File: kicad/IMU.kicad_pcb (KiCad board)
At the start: 4 copper layers, 30 x 30 mm, 85 parts, among them IC1 FT232RQ, P1 M1P, P10 CONN_01X02, P11 CONN_02X05, P12 CONN_02X06, P2 M1N, P3 M3P, P4 M3N, P5 JTAG_DB, P6 M2P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

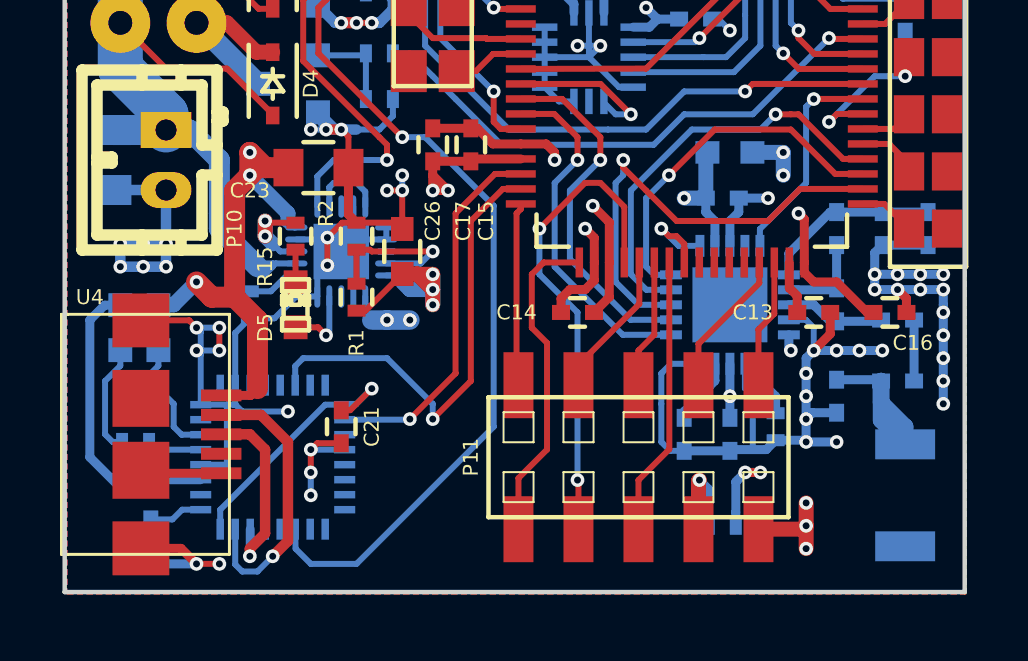
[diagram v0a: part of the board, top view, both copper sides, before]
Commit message: Moved USB and external edge connector and re-routed FTDI IC.
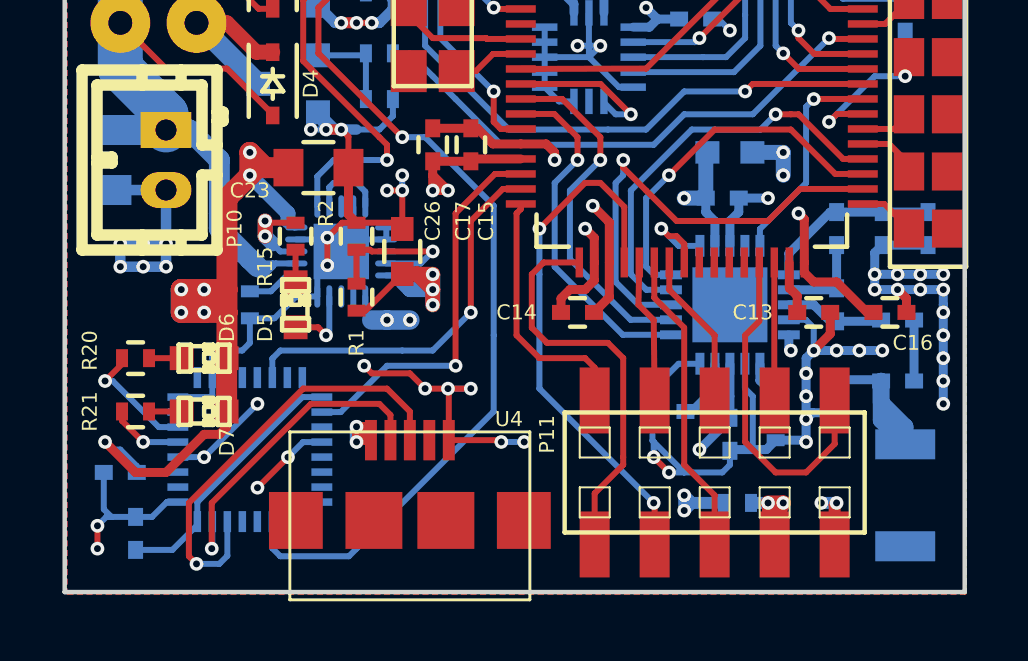
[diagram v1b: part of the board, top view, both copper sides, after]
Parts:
- added G***: LOGO, logos:Panda_Logo_4x3mm, B.Cu at (115.1, 97.3)
- C21: moved to B.Cu
- D6, D7, R20, R21: moved to F.Cu
- moved U4 11.3 mm to (111.5, 99.1), turned to 0 degrees
- moved C21 7.73 mm to (102.4, 98.0), turned to 90 degrees
- moved D7 3.95 mm to (104.6, 94.0), turned to 180 degrees
- moved P11 2.59 mm to (121.7, 96.0)
- moved D6 1.83 mm to (104.6, 92.2), turned to 180 degrees
- moved C22 1.44 mm to (101.9, 96.0), turned to 180 degrees
- moved R20 1.27 mm to (102.4, 92.2), turned to 0 degrees
- moved R21 1.02 mm to (102.4, 94.0), turned to 0 degrees
- moved C2 0.92 mm to (120.1, 94.0), turned to 180 degrees
- moved R16 0.92 mm to (122.4, 97.0), turned to 0 degrees
- moved IC1 0.80 mm to (106.2, 95.2)
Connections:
- P11 pad 10: /Microcontroller/CON_SDA -> /Microcontroller/CON_SCL
- P11 pad 5: /Microcontroller/CON_MOSI -> /Microcontroller/CON_MISO
- P11 pad 6: /Microcontroller/CON_MISO -> /Microcontroller/CON_MOSI
- P11 pad 8: /Microcontroller/CON_SCL -> /Microcontroller/CON_SDA
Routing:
- net +5V: track 29.3 -> 49.0 mm, vias 3 -> 9
- net Net-(IC1-Pad14): track 6.35 -> 14.6 mm
- net /Microcontroller/CON_SCL: track 4.93 -> 11.4 mm
- net /Microcontroller/CON_MISO: track 4.31 -> 10.2 mm
- net GND: track 178.8 -> 174.5 mm, vias 88 -> 90
- net /Microcontroller/CON_MOSI: track 9.32 -> 5.23 mm
- net Net-(C3-Pad1): track 15.7 -> 19.4 mm
- net /Microcontroller/CON_RX: track 10.8 -> 13.6 mm
- net /Power/FTDI_TXD: track 15.7 -> 13.0 mm
- net Net-(D7-Pad2): track 3.69 -> 1.09 mm
- net /Microcontroller/CON_TX: track 6.13 -> 8.58 mm
- net /Microcontroller/CON_DAC: track 16.2 -> 17.8 mm
- net Net-(IC1-Pad15): track 9.35 -> 10.8 mm
- net Net-(IC1-Pad22): track 2.70 -> 4.06 mm, vias 0 -> 1
- net Net-(D6-Pad2): track 2.34 -> 1.09 mm
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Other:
- board text added: "Jonas A 2015"

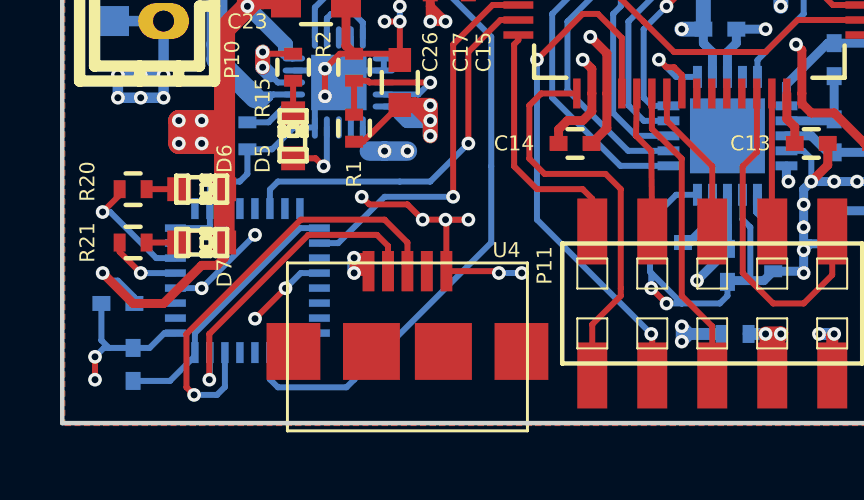
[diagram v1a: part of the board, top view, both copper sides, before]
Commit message: Replaced USB connector footprint.
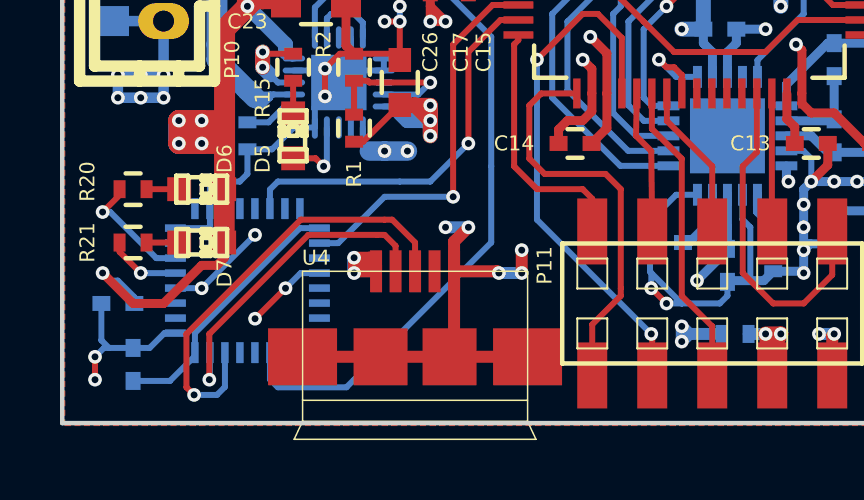
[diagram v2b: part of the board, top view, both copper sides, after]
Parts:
- U4: footprint open-project:MICRO-B_USB -> USB-B-Micro:USB-B-Micro
- moved U4 1.30 mm to (111.8, 97.8)
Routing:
- net GND: track 174.5 -> 181.5 mm, vias 90 -> 89
- net +5V: track 49.0 -> 49.5 mm

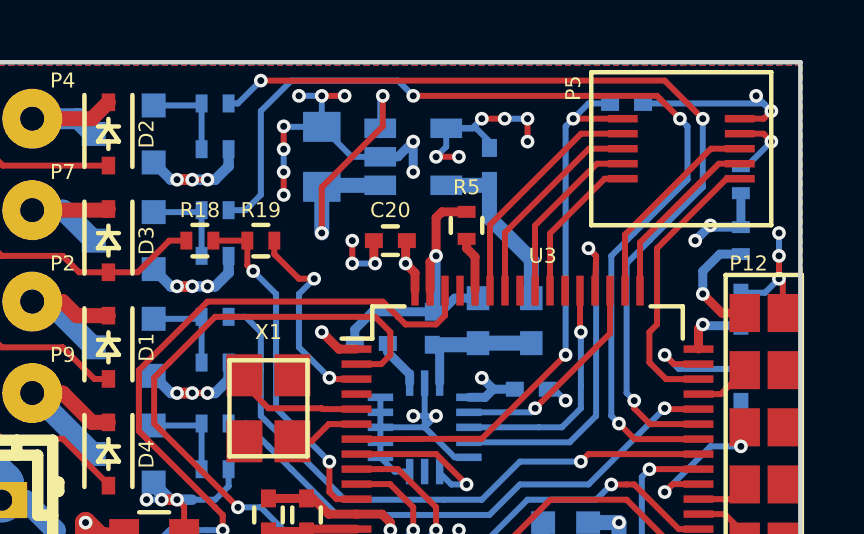
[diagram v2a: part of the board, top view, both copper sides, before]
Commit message: Added debug LED to mcu pin.
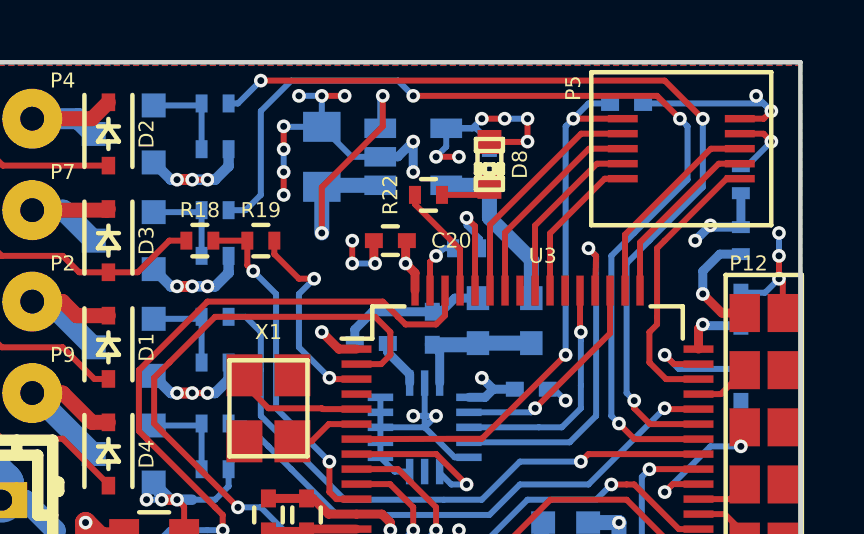
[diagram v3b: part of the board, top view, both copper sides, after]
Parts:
- added D8: LED, LEDs:LED-0603, F.Cu at (119.6, 73.4)
- added R22: 2k2, Resistors_SMD:R_0402, F.Cu at (117.6, 74.4)
- R5: moved to B.Cu
- moved R5 0.76 mm to (118.9, 76.2), turned to 0 degrees
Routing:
- net Net-(R22-Pad1): track 0.00 -> 3.81 mm
- net GND: track 181.5 -> 179.3 mm
- net Net-(R5-Pad2): track 1.84 -> 3.75 mm, vias 0 -> 1
- net Net-(D8-Pad1): track 0.00 -> 1.69 mm

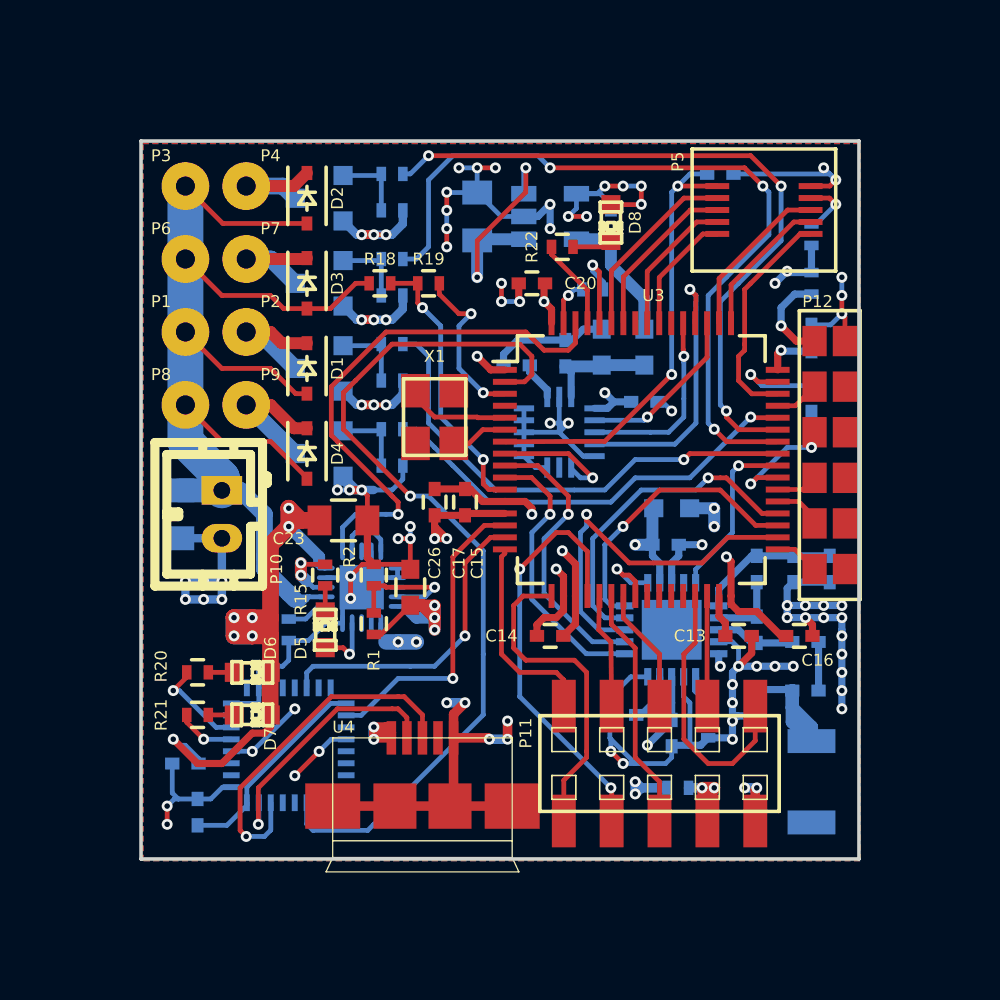
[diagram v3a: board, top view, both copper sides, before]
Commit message: Cleared corner areas to allow for arm attachments.
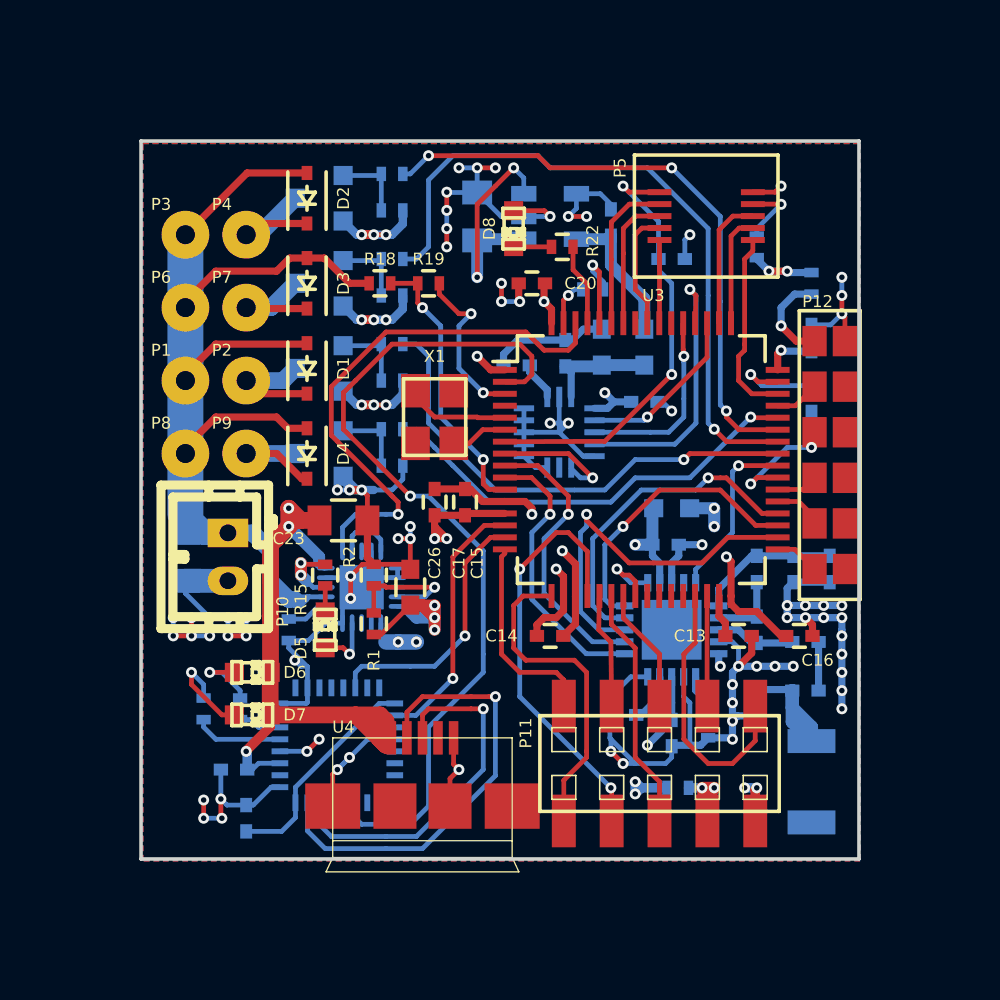
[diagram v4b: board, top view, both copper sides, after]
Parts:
- R20, R21: moved to B.Cu
- moved C18 4.10 mm to (122.2, 74.9)
- moved D8 4.07 mm to (115.6, 73.7)
- moved P5 2.43 mm to (121.7, 72.1)
- moved R20 2.34 mm to (104.1, 93.7), turned to 90 degrees
- moved R14 2.34 mm to (125.7, 74.4)
- moved C21 2.05 mm to (104.4, 98.3)
- moved C22 2.05 mm to (103.9, 96.3)
- moved P1 2.03 mm to (101.9, 80.0)
- moved P2 2.03 mm to (104.4, 80.0)
- moved P8 2.03 mm to (101.9, 83.1)
- moved P9 2.03 mm to (104.4, 83.1)
- moved IC1 2.03 mm to (108.2, 95.2)
- moved P3 2.03 mm to (101.9, 73.9)
- moved P4 2.03 mm to (104.4, 73.9)
- moved P6 2.03 mm to (101.9, 77.0)
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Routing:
- net +5V: track 49.5 -> 27.9 mm, vias 9 -> 3
- net GND: track 179.3 -> 162.7 mm, vias 89 -> 87
- net Net-(IC1-Pad15): track 11.0 -> 18.9 mm
- net /Microcontroller/M2: track 33.3 -> 28.8 mm, vias 3 -> 1
- net /Microcontroller/M3: track 29.8 -> 25.5 mm
- net Net-(D7-Pad2): track 1.09 -> 4.11 mm, vias 0 -> 1
- net Net-(IC1-Pad22): track 4.06 -> 1.80 mm, vias 1 -> 0
- net /Power/FTDI_TXD: track 13.0 -> 11.0 mm
- net /Power/FTDI_RXD: track 12.9 -> 10.9 mm
- net Net-(D6-Pad2): track 1.09 -> 2.93 mm, vias 0 -> 1
- net /Microcontroller/TDO/SWO: track 5.09 -> 3.48 mm
- net /Microcontroller/TMS/SWDIO: track 9.50 -> 7.99 mm
- net /Microcontroller/PWREN#: track 37.6 -> 36.1 mm
- net /Microcontroller/DB_RX: track 7.89 -> 6.55 mm
- net /Microcontroller/TDI: track 6.88 -> 5.55 mm
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
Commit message: Added shoulders for arms at corners.
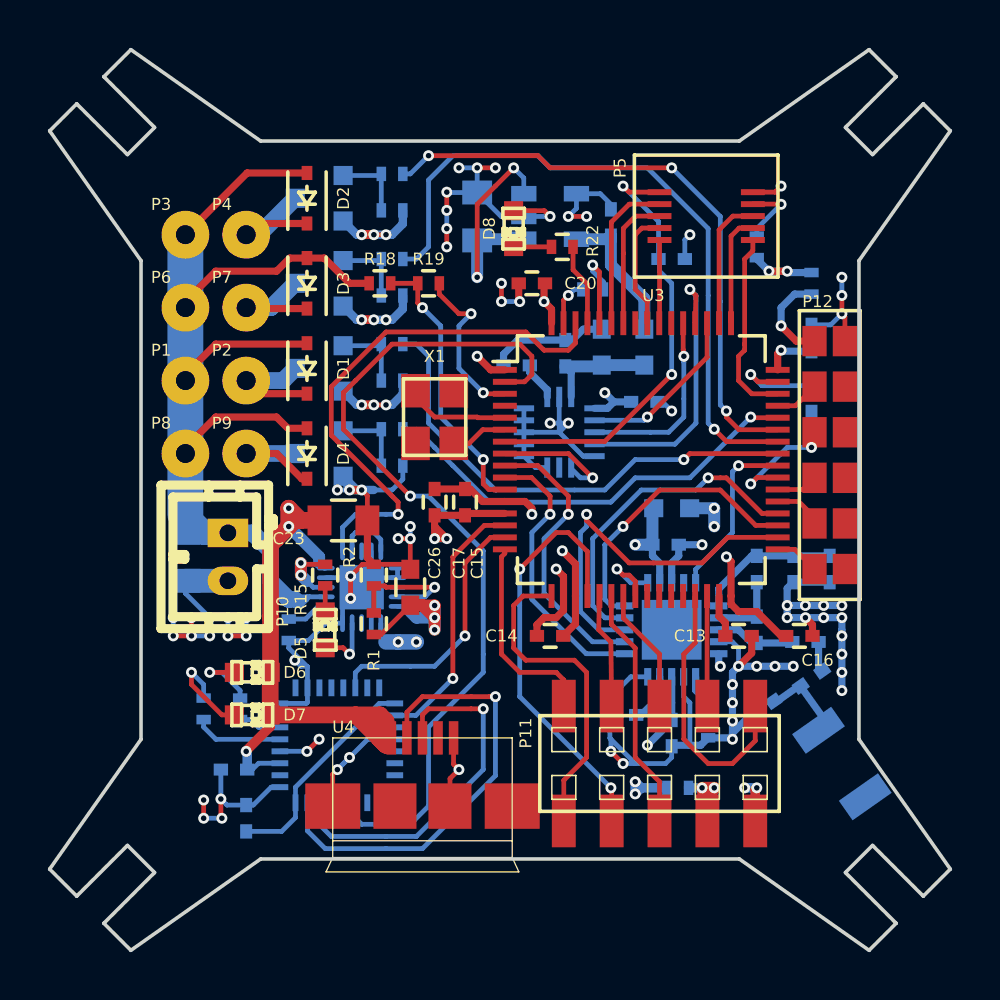
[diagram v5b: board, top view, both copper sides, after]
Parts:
- moved G*** 2.05 mm to (116.3, 96.0)
- moved Y1 1.48 mm to (129.3, 96.0), turned to 125.1 degrees
- moved C8 0.57 mm to (128.0, 92.5), turned to 35.1 degrees
- moved C11 0.36 mm to (126.0, 93.7), turned to 35.1 degrees
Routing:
- net Net-(C11-Pad2): track 6.39 -> 3.61 mm
- net Net-(C8-Pad2): track 2.03 -> 1.27 mm
- net GND: track 162.7 -> 161.9 mm, vias 87 -> 86
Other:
- board size 30 x 30 mm -> 37.6 x 37.6 mm

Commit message: Add solder pads to arm-mountings.
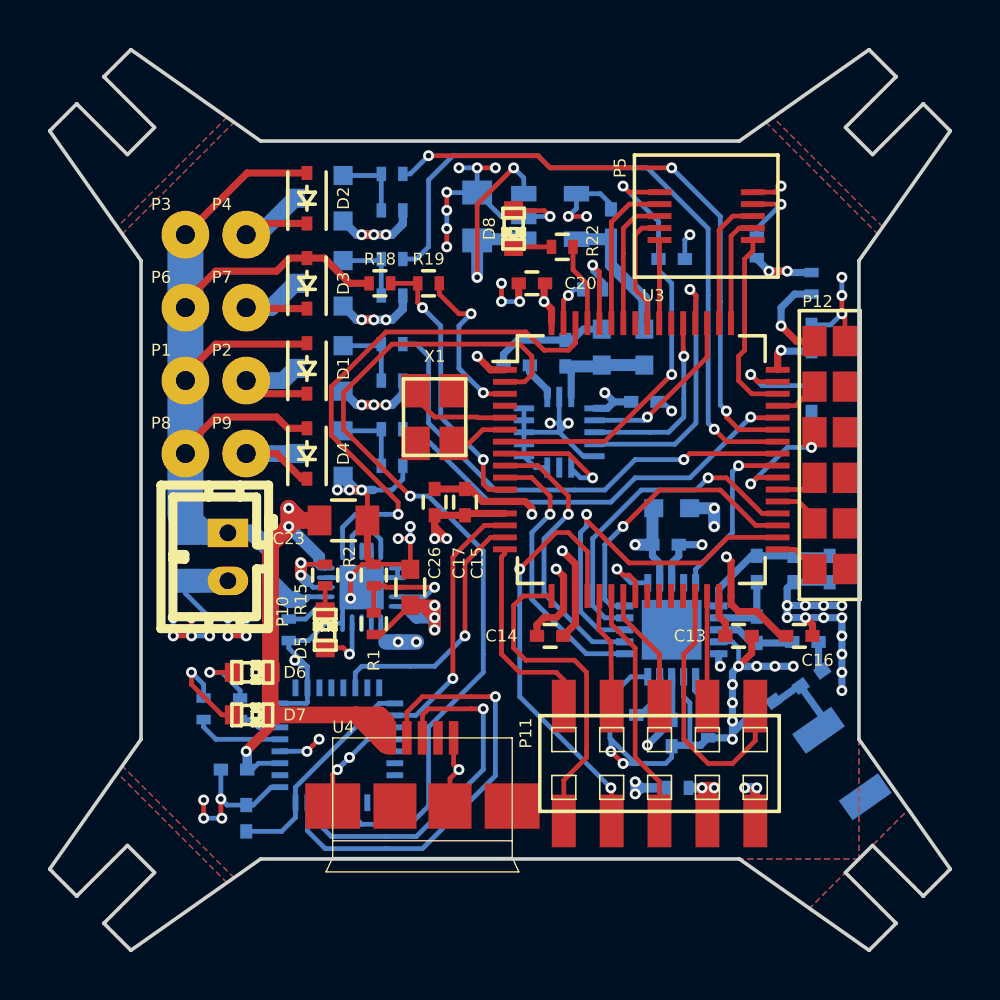
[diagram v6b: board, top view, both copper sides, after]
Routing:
- added copper zone on B.Cu, net (none)
- added copper zone on F.Cu, net (none)

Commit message: Change clearance of power planes and add logos. Generate BOM.
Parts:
- added G***: LOGO, logos:IMU_Logo_6x3mm, B.Cu at (116.3, 96.8)
- moved G*** 27.5 mm to (128.5, 71.4), turned to 315 degrees
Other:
- board text added: "Rev A"
